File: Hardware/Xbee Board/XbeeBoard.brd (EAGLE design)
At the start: 2 parts

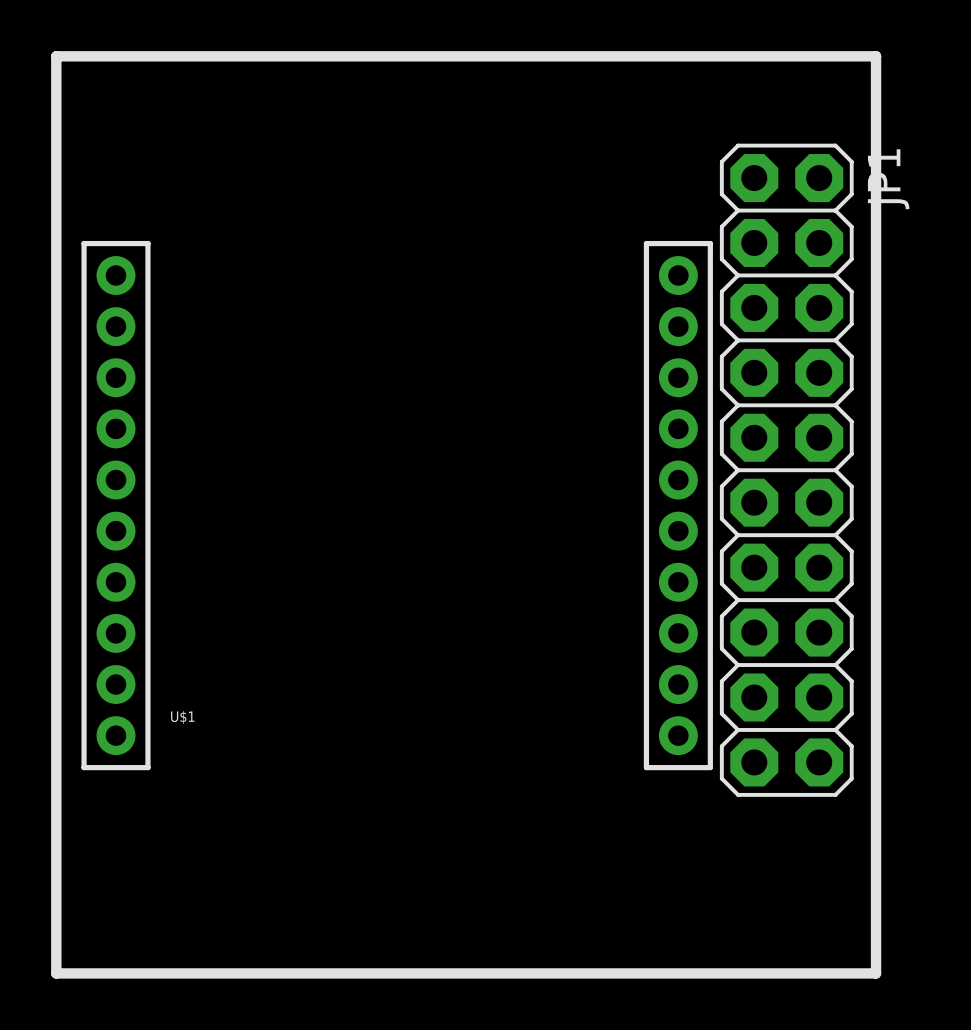
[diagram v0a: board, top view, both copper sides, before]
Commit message: updated boards + logo 6 in illustrator
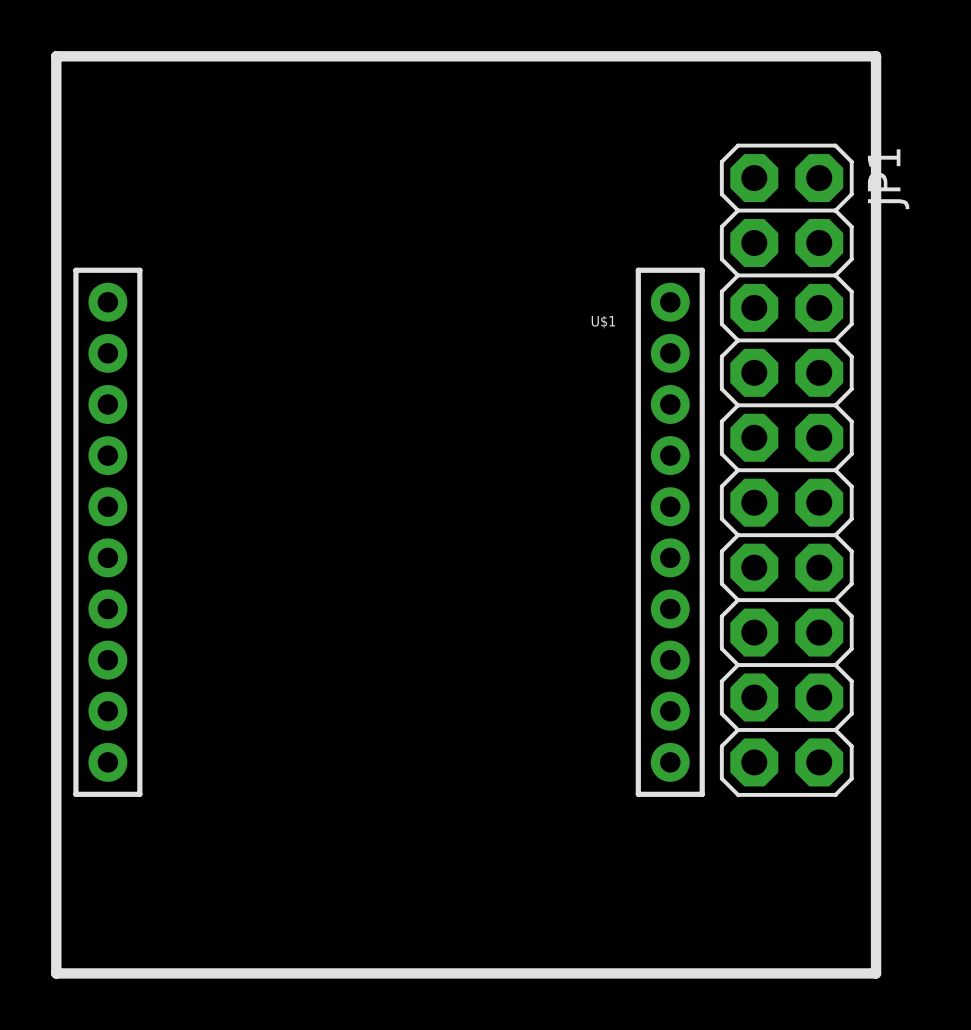
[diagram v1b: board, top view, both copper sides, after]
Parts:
- moved U$1 21.0 mm to (13.7, 71.8), turned to 180 degrees
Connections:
- removed net GND: U$1.10
- removed net VDD: U$1.1
- new net N$1: JP1.1, U$1.1
- new net N$2: JP1.10, U$1.2
- new net N$3: JP1.8, U$1.3
- new net N$4: JP1.6, U$1.10
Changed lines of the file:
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@@
 </autorouter>
 <elements>
-<element name="U$1" library="SparkFun-RF" package="XBEE-1" value="XBEE-2B1" x="13.97" y="50.8"/>
+<element name="U$1" library="SparkFun-RF" package="XBEE-1" value="XBEE-2B1" x="13.6525" y="71.755" rot="R180"/>
 <element name="JP1" library="SparkFun-Connectors" package="2X10" value="" x="29.21" y="63.1825" rot="R270"/>
 </elements>
 <signals>
-<signal name="VDD">
+<signal name="N$1">
 <contactref element="U$1" pad="1"/>
+<contactref element="JP1" pad="1"/>
+<wire x1="24.6525" y1="51.755" x2="27.94" y2="74.6125" width="0" layer="19" extent="1-1"/>
 </signal>
-<signal name="GND">
+<signal name="N$2">
+<contactref element="U$1" pad="2"/>
+<contactref element="JP1" pad="10"/>
+<wire x1="24.6525" y1="53.755" x2="30.48" y2="64.4525" width="0" layer="19" extent="1-1"/>
+</signal>
+<signal name="N$3">
+<contactref element="U$1" pad="3"/>
+<contactref element="JP1" pad="8"/>
+<wire x1="24.6525" y1="55.755" x2="30.48" y2="66.9925" width="0" layer="19" extent="1-1"/>
+</signal>
+<signal name="N$4">
 <contactref element="U$1" pad="10"/>
+<contactref element="JP1" pad="6"/>
+<wire x1="24.6525" y1="69.755" x2="30.48" y2="69.5325" width="0" layer="19" extent="1-1"/>
 </signal>
 </signals>
